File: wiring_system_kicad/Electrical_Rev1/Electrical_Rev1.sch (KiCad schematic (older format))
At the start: 1 part

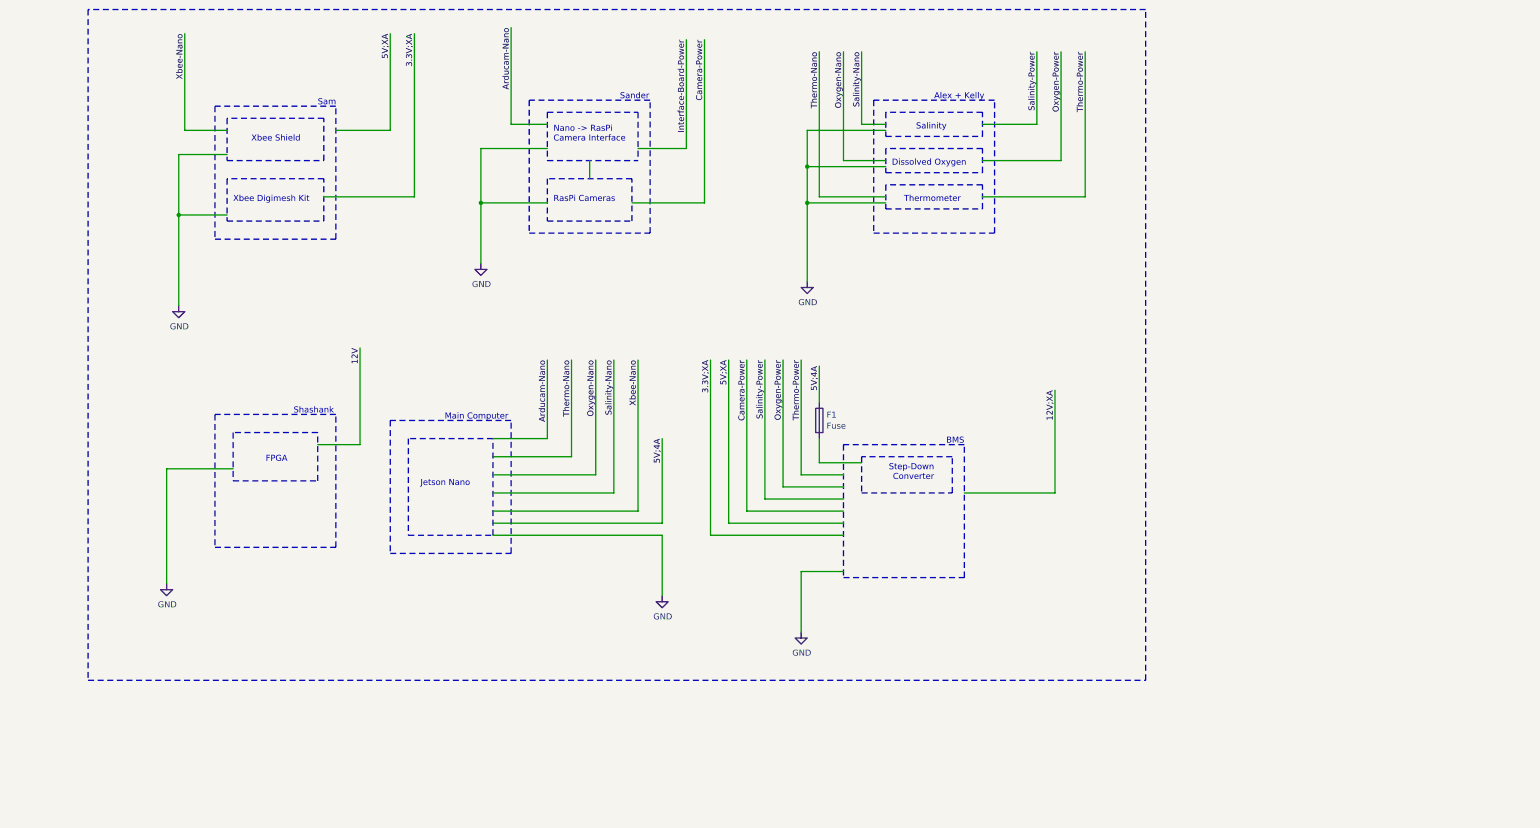
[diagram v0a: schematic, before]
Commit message: Add KiCAD files for wiring diagram
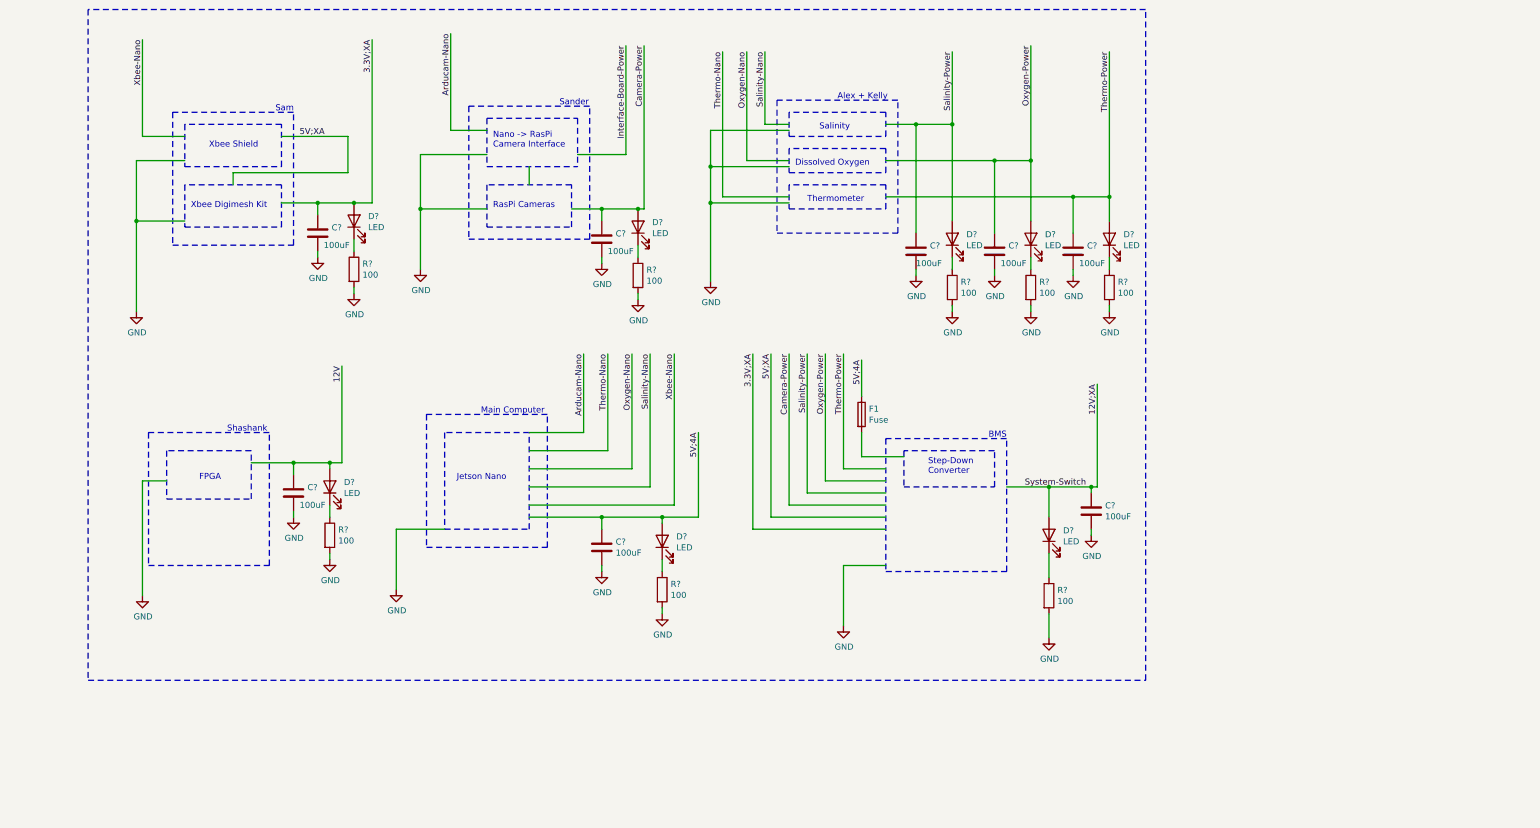
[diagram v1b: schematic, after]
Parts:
- added C? (x8): 100uF, symbol Device:C
- added D? (x8): LED, symbol Device:LED
- added R? (x8): 100, symbol Device:R
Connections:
- net labels added: System-Switch
- wire segments 76 -> 129
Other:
- moved on the sheet: F1

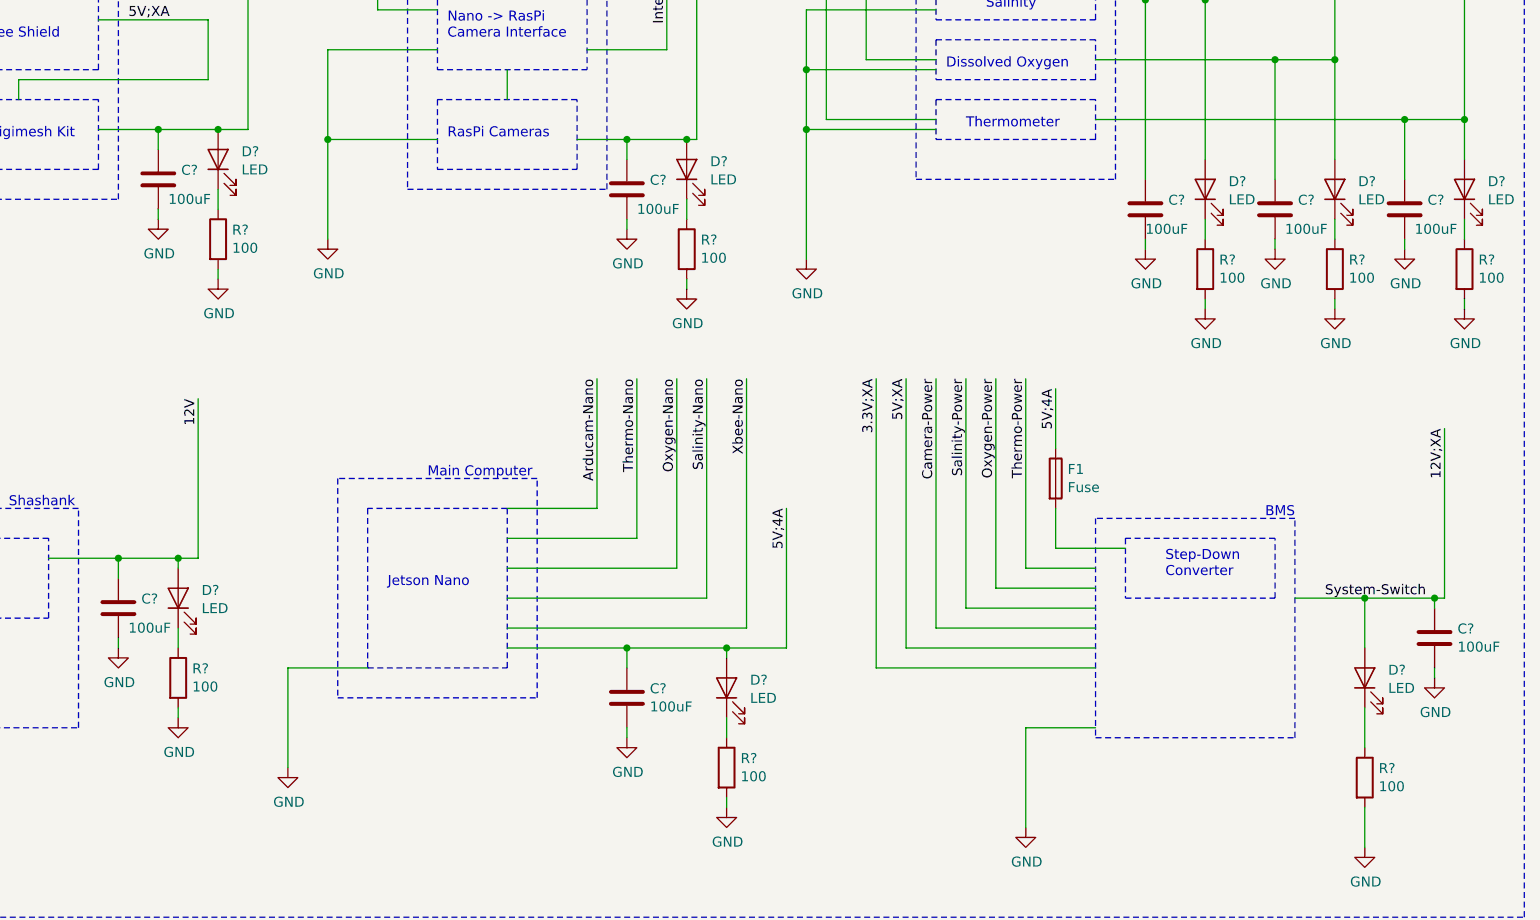
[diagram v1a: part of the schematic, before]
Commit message: Fix component references
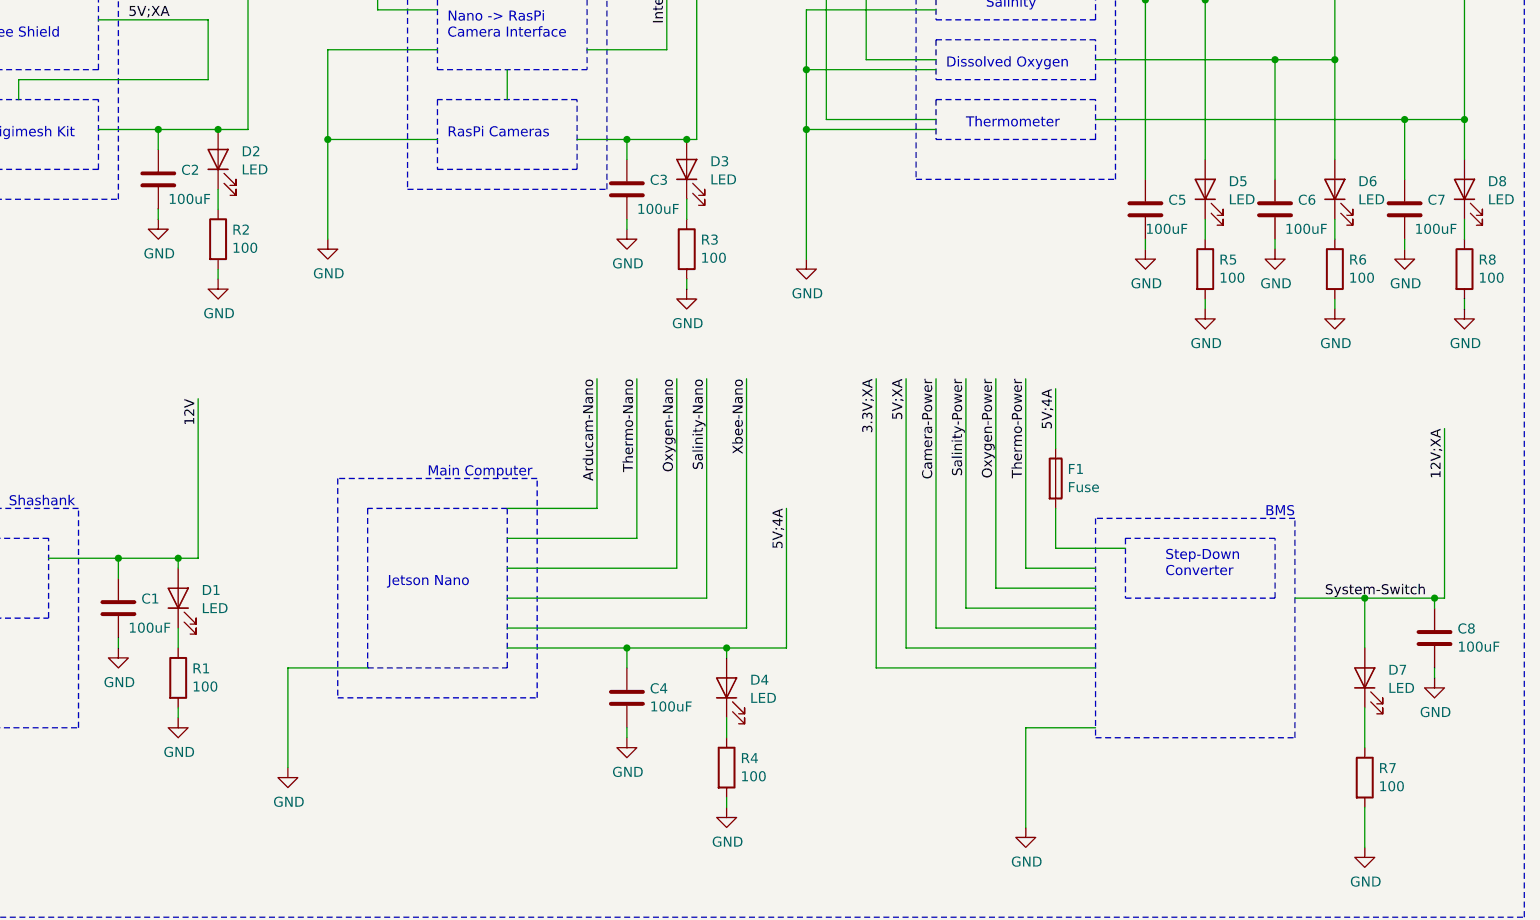
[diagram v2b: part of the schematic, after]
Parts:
- gave numbers to parts that had none: 24
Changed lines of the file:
@@
 	9350 4750 9700 4750
 $Comp
-L Device:LED D?
+L Device:LED D7
 U 1 1 5F9DA263
 P 9350 5150
-F 0 "D?" V 9389 5033 50  0000 R CNN
+F 0 "D7" V 9389 5033 50  0000 R CNN
 F 1 "LED" V 9298 5033 50  0000 R CNN
 F 2 "" H 9350 5150 50  0001 C CNN
@@
 $EndComp
 $Comp
-L Device:R R?
+L Device:R R7
 U 1 1 5F9DA8CB
 P 9350 5650
-F 0 "R?" H 9420 5696 50  0000 L CNN
+F 0 "R7" H 9420 5696 50  0000 L CNN
 F 1 "100" H 9420 5605 50  0000 L CNN
 F 2 "" V 9280 5650 50  0001 C CNN
@@
 $EndComp
 $Comp
-L power:GND #PWR?
+L power:GND #PWR019
 U 1 1 5F9DAB7C
 P 9350 6000
-F 0 "#PWR?" H 9350 5750 50  0001 C CNN
+F 0 "#PWR019" H 9350 5750 50  0001 C CNN
 F 1 "GND" H 9355 5827 50  0000 C CNN
 F 2 "" H 9350 6000 50  0001 C CNN
@@
 	3950 5100 4350 5100
 $Comp
-L Device:C C?
+L Device:C C4
 U 1 1 5F9E7052
 P 5650 5250
-F 0 "C?" H 5765 5296 50  0000 L CNN
+F 0 "C4" H 5765 5296 50  0000 L CNN
 F 1 "100uF" H 5765 5205 50  0000 L CNN
 F 2 "" H 5688 5100 50  0001 C CNN
@@
 $EndComp
 $Comp
-L Device:LED D?
+L Device:LED D4
 U 1 1 5F9E9779
 P 6150 5200
-F 0 "D?" V 6189 5083 50  0000 R CNN
+F 0 "D4" V 6189 5083 50  0000 R CNN
 F 1 "LED" V 6098 5083 50  0000 R CNN
 F 2 "" H 6150 5200 50  0001 C CNN
@@
 $EndComp
 $Comp
-L Device:R R?
+L Device:R R4
 U 1 1 5F9E977F
 P 6150 5600
-F 0 "R?" H 6220 5646 50  0000 L CNN
+F 0 "R4" H 6220 5646 50  0000 L CNN
 F 1 "100" H 6220 5555 50  0000 L CNN
 F 2 "" V 6080 5600 50  0001 C CNN
@@
 $EndComp
 $Comp
-L power:GND #PWR?
+L power:GND #PWR012
 U 1 1 5F9E9785
 P 5650 5450
-F 0 "#PWR?" H 5650 5200 50  0001 C CNN
+F 0 "#PWR012" H 5650 5200 50  0001 C CNN
 F 1 "GND" H 5655 5277 50  0000 C CNN
 F 2 "" H 5650 5450 50  0001 C CNN
@@
 	5650 5000 6150 5000
 $Comp
-L power:GND #PWR?
+L power:GND #PWR014
 U 1 1 5FA0B098
 P 6150 5800
-F 0 "#PWR?" H 6150 5550 50  0001 C CNN
+F 0 "#PWR014" H 6150 5550 50  0001 C CNN
 F 1 "GND" H 6155 5627 50  0000 C CNN
 F 2 "" H 6150 5800 50  0001 C CNN
@@
 	2750 4550 3100 4550
 $Comp
-L Device:C C?
+L Device:C C1
 U 1 1 5FA36B80
 P 3100 4800
-F 0 "C?" H 3215 4846 50  0000 L CNN
+F 0 "C1" H 3215 4846 50  0000 L CNN
 F 1 "100uF" H 3150 4700 50  0000 L CNN
 F 2 "" H 3138 4650 50  0001 C CNN
@@
 $EndComp
 $Comp
-L Device:LED D?
+L Device:LED D1
 U 1 1 5FA36B86
 P 3400 4750
-F 0 "D?" V 3439 4633 50  0000 R CNN
+F 0 "D1" V 3439 4633 50  0000 R CNN
 F 1 "LED" V 3348 4633 50  0000 R CNN
 F 2 "" H 3400 4750 50  0001 C CNN
@@
 $EndComp
 $Comp
-L Device:R R?
+L Device:R R1
 U 1 1 5FA36B8C
 P 3400 5150
-F 0 "R?" H 3470 5196 50  0000 L CNN
+F 0 "R1" H 3470 5196 50  0000 L CNN
 F 1 "100" H 3470 5105 50  0000 L CNN
 F 2 "" V 3330 5150 50  0001 C CNN
@@
 $EndComp
 $Comp
-L power:GND #PWR?
+L power:GND #PWR07
 U 1 1 5FA36B92
 P 3100 5000
-F 0 "#PWR?" H 3100 4750 50  0001 C CNN
+F 0 "#PWR07" H 3100 4750 50  0001 C CNN
 F 1 "GND" H 3105 4827 50  0000 C CNN
 F 2 "" H 3100 5000 50  0001 C CNN
@@
 	3100 4650 3100 4550
 $Comp
-L power:GND #PWR?
+L power:GND #PWR09
 U 1 1 5FA36B9C
 P 3400 5350
-F 0 "#PWR?" H 3400 5100 50  0001 C CNN
+F 0 "#PWR09" H 3400 5100 50  0001 C CNN
 F 1 "GND" H 3405 5177 50  0000 C CNN
 F 2 "" H 3400 5350 50  0001 C CNN
@@
 	3600 3100 3600 3150
 $Comp
-L power:GND #PWR?
+L power:GND #PWR010
 U 1 1 5FA43884
 P 3600 3150
-F 0 "#PWR?" H 3600 2900 50  0001 C CNN
+F 0 "#PWR010" H 3600 2900 50  0001 C CNN
 F 1 "GND" H 3605 2977 50  0000 C CNN
 F 2 "" H 3600 3150 50  0001 C CNN
@@
 	3600 2700 3600 2800
 $Comp
-L power:GND #PWR?
+L power:GND #PWR08
 U 1 1 5FA4387B
 P 3300 2850
-F 0 "#PWR?" H 3300 2600 50  0001 C CNN
+F 0 "#PWR08" H 3300 2600 50  0001 C CNN
 F 1 "GND" H 3305 2677 50  0000 C CNN
 F 2 "" H 3300 2850 50  0001 C CNN
@@
 $EndComp
 $Comp
-L Device:R R?
+L Device:R R2
 U 1 1 5FA43875
 P 3600 2950
-F 0 "R?" H 3670 2996 50  0000 L CNN
+F 0 "R2" H 3670 2996 50  0000 L CNN
 F 1 "100" H 3670 2905 50  0000 L CNN
 F 2 "" V 3530 2950 50  0001 C CNN
@@
 $EndComp
 $Comp
-L Device:LED D?
+L Device:LED D2
 U 1 1 5FA4386F
 P 3600 2550
-F 0 "D?" V 3639 2433 50  0000 R CNN
+F 0 "D2" V 3639 2433 50  0000 R CNN
 F 1 "LED" V 3548 2433 50  0000 R CNN
 F 2 "" H 3600 2550 50  0001 C CNN
@@
 $EndComp
 $Comp
-L Device:C C?
+L Device:C C2
 U 1 1 5FA43869
 P 3300 2650
-F 0 "C?" H 3415 2696 50  0000 L CNN
+F 0 "C2" H 3415 2696 50  0000 L CNN
 F 1 "100uF" H 3350 2550 50  0000 L CNN
 F 2 "" H 3338 2500 50  0001 C CNN
@@
 	5950 3150 5950 3200
 $Comp
-L power:GND #PWR?
+L power:GND #PWR013
 U 1 1 5FA6126C
 P 5950 3200
-F 0 "#PWR?" H 5950 2950 50  0001 C CNN
+F 0 "#PWR013" H 5950 2950 50  0001 C CNN
 F 1 "GND" H 5955 3027 50  0000 C CNN
 F 2 "" H 5950 3200 50  0001 C CNN
@@
 	5950 2750 5950 2850
 $Comp
-L power:GND #PWR?
+L power:GND #PWR011
 U 1 1 5FA61275
 P 5650 2900
-F 0 "#PWR?" H 5650 2650 50  0001 C CNN
+F 0 "#PWR011" H 5650 2650 50  0001 C CNN
 F 1 "GND" H 5655 2727 50  0000 C CNN
 F 2 "" H 5650 2900 50  0001 C CNN
@@
 $EndComp
 $Comp
-L Device:R R?
+L Device:R R3
 U 1 1 5FA6127B
 P 5950 3000
-F 0 "R?" H 6020 3046 50  0000 L CNN
+F 0 "R3" H 6020 3046 50  0000 L CNN
 F 1 "100" H 6020 2955 50  0000 L CNN
 F 2 "" V 5880 3000 50  0001 C CNN
@@
 $EndComp
 $Comp
-L Device:LED D?
+L Device:LED D3
 U 1 1 5FA61281
 P 5950 2600
-F 0 "D?" V 5989 2483 50  0000 R CNN
+F 0 "D3" V 5989 2483 50  0000 R CNN
 F 1 "LED" V 5898 2483 50  0000 R CNN
 F 2 "" H 5950 2600 50  0001 C CNN
@@
 $EndComp
 $Comp
-L Device:C C?
+L Device:C C3
 U 1 1 5FA61287
 P 5650 2700
-F 0 "C?" H 5765 2746 50  0000 L CNN
+F 0 "C3" H 5765 2746 50  0000 L CNN
 F 1 "100uF" H 5700 2600 50  0000 L CNN
 F 2 "" H 5688 2550 50  0001 C CNN
@@
 	5950 2450 6000 2450
 $Comp
-L Device:C C?
+L Device:C C8
 U 1 1 5FA7A0A9
 P 9700 4950
-F 0 "C?" H 9815 4996 50  0000 L CNN
+F 0 "C8" H 9815 4996 50  0000 L CNN
 F 1 "100uF" H 9815 4905 50  0000 L CNN
 F 2 "" H 9738 4800 50  0001 C CNN
@@
 $EndComp
 $Comp
-L power:GND #PWR?
+L power:GND #PWR021
 U 1 1 5FA7A0AF
 P 9700 5150
-F 0 "#PWR?" H 9700 4900 50  0001 C CNN
+F 0 "#PWR021" H 9700 4900 50  0001 C CNN
 F 1 "GND" H 9705 4977 50  0000 C CNN
 F 2 "" H 9700 5150 50  0001 C CNN
@@
 	9850 3250 9850 3300
 $Comp
-L power:GND #PWR?
+L power:GND #PWR022
 U 1 1 5FAB1E80
 P 9850 3300
-F 0 "#PWR?" H 9850 3050 50  0001 C CNN
+F 0 "#PWR022" H 9850 3050 50  0001 C CNN
 F 1 "GND" H 9855 3127 50  0000 C CNN
 F 2 "" H 9850 3300 50  0001 C CNN
@@
 	9850 2850 9850 2950
 $Comp
-L power:GND #PWR?
+L power:GND #PWR020
 U 1 1 5FAB1E89
 P 9550 3000
-F 0 "#PWR?" H 9550 2750 50  0001 C CNN
+F 0 "#PWR020" H 9550 2750 50  0001 C CNN
 F 1 "GND" H 9555 2827 50  0000 C CNN
 F 2 "" H 9550 3000 50  0001 C CNN
@@
 $EndComp
 $Comp
-L Device:R R?
+L Device:R R8
 U 1 1 5FAB1E8F
 P 9850 3100
-F 0 "R?" H 9920 3146 50  0000 L CNN
+F 0 "R8" H 9920 3146 50  0000 L CNN
 F 1 "100" H 9920 3055 50  0000 L CNN
 F 2 "" V 9780 3100 50  0001 C CNN
@@
 $EndComp
 $Comp
-L Device:LED D?
+L Device:LED D8
 U 1 1 5FAB1E95
 P 9850 2700
-F 0 "D?" V 9889 2583 50  0000 R CNN
+F 0 "D8" V 9889 2583 50  0000 R CNN
 F 1 "LED" V 9798 2583 50  0000 R CNN
 F 2 "" H 9850 2700 50  0001 C CNN
@@
 $EndComp
 $Comp
-L Device:C C?
+L Device:C C7
 U 1 1 5FAB1E9B
 P 9550 2800
-F 0 "C?" H 9665 2846 50  0000 L CNN
+F 0 "C7" H 9665 2846 50  0000 L CNN
 F 1 "100uF" H 9600 2700 50  0000 L CNN
 F 2 "" H 9588 2650 50  0001 C CNN
@@
 	9200 3250 9200 3300
 $Comp
-L power:GND #PWR?
+L power:GND #PWR018
 U 1 1 5FAB82C3
 P 9200 3300
-F 0 "#PWR?" H 9200 3050 50  0001 C CNN
+F 0 "#PWR018" H 9200 3050 50  0001 C CNN
 F 1 "GND" H 9205 3127 50  0000 C CNN
 F 2 "" H 9200 3300 50  0001 C CNN
@@
 	9200 2850 9200 2950
 $Comp
-L power:GND #PWR?
+L power:GND #PWR017
 U 1 1 5FAB82CC
 P 8900 3000
-F 0 "#PWR?" H 8900 2750 50  0001 C CNN
+F 0 "#PWR017" H 8900 2750 50  0001 C CNN
 F 1 "GND" H 8905 2827 50  0000 C CNN
 F 2 "" H 8900 3000 50  0001 C CNN
@@
 $EndComp
 $Comp
-L Device:R R?
+L Device:R R6
 U 1 1 5FAB82D2
 P 9200 3100
-F 0 "R?" H 9270 3146 50  0000 L CNN
+F 0 "R6" H 9270 3146 50  0000 L CNN
 F 1 "100" H 9270 3055 50  0000 L CNN
 F 2 "" V 9130 3100 50  0001 C CNN
@@
 $EndComp
 $Comp
-L Device:LED D?
+L Device:LED D6
 U 1 1 5FAB82D8
 P 9200 2700
-F 0 "D?" V 9239 2583 50  0000 R CNN
+F 0 "D6" V 9239 2583 50  0000 R CNN
 F 1 "LED" V 9148 2583 50  0000 R CNN
 F 2 "" H 9200 2700 50  0001 C CNN
@@
 $EndComp
 $Comp
-L Device:C C?
+L Device:C C6
 U 1 1 5FAB82DE
 P 8900 2800
-F 0 "C?" H 9015 2846 50  0000 L CNN
+F 0 "C6" H 9015 2846 50  0000 L CNN
 F 1 "100uF" H 8950 2700 50  0000 L CNN
 F 2 "" H 8938 2650 50  0001 C CNN
@@
 	8550 3250 8550 3300
 $Comp
-L power:GND #PWR?
+L power:GND #PWR016
 U 1 1 5FADF758
 P 8550 3300
-F 0 "#PWR?" H 8550 3050 50  0001 C CNN
+F 0 "#PWR016" H 8550 3050 50  0001 C CNN
 F 1 "GND" H 8555 3127 50  0000 C CNN
 F 2 "" H 8550 3300 50  0001 C CNN
@@
 	8550 2850 8550 2950
 $Comp
-L power:GND #PWR?
+L power:GND #PWR015
 U 1 1 5FADF761
 P 8250 3000
-F 0 "#PWR?" H 8250 2750 50  0001 C CNN
+F 0 "#PWR015" H 8250 2750 50  0001 C CNN
 F 1 "GND" H 8255 2827 50  0000 C CNN
 F 2 "" H 8250 3000 50  0001 C CNN
@@
 $EndComp
 $Comp
-L Device:R R?
+L Device:R R5
 U 1 1 5FADF767
 P 8550 3100
-F 0 "R?" H 8620 3146 50  0000 L CNN
+F 0 "R5" H 8620 3146 50  0000 L CNN
 F 1 "100" H 8620 3055 50  0000 L CNN
 F 2 "" V 8480 3100 50  0001 C CNN
@@
 $EndComp
 $Comp
-L Device:LED D?
+L Device:LED D5
 U 1 1 5FADF76D
 P 8550 2700
-F 0 "D?" V 8589 2583 50  0000 R CNN
+F 0 "D5" V 8589 2583 50  0000 R CNN
 F 1 "LED" V 8498 2583 50  0000 R CNN
 F 2 "" H 8550 2700 50  0001 C CNN
@@
 $EndComp
 $Comp
-L Device:C C?
+L Device:C C5
 U 1 1 5FADF773
 P 8250 2800
-F 0 "C?" H 8365 2846 50  0000 L CNN
+F 0 "C5" H 8365 2846 50  0000 L CNN
 F 1 "100uF" H 8250 2700 50  0000 L CNN
 F 2 "" H 8288 2650 50  0001 C CNN
